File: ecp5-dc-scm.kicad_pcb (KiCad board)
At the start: 6 copper layers, 90 x 120.4 mm, 361 parts, among them IC1 TPS54561, J1 12V_EXT, J10 61301021121, J11 1-2199230-6, J2 S2B-PH-K-S_LF__SN_, J3 2X05, J4 61301021121, J5 61301021121, J6 61301221121, J7 61300611121, J8 SFF-TA-1002-4C+, J9 543630489, Q1 2N7002, Q2 2N7002, Q3 2N7002, Q4 2N7002, Q5 2N7002, Q6 2N7002, Q7 2N7002, U1 ECP5UM5G_85_CABGA756, U10 TPS62823DLCT, U11 W25Q32JVSSIQ_TR, U12 TPS51200DRC, U13 AS4C256M16D3, U14 W25Q32JVSSIQ_TR, U15 W25Q32JVSSIQ_TR, U16 W25Q32JVSSIQ_TR, U2 KSZ9031RNXCA, U3 LM3881MME_NOPB, U4 LM21212-2, U5 TPS71710DCKT, U6 NVT2008DQ,115, U7 TPS62823DLCT, U8 TPS62823DLCT, U9 TPS62823DLCT, Y1 ABM8G-25.000MHZ-18-D2Y-T

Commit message: Add initial component placement
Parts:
- removed the R66 at (353.6, 117.9)
- removed the U16 at (382.4, 132.6)
- removed the U6 at (372.8, 115.2)
- added R53: R_10k_0402, antmicro-footprints:0402-res, F.Cu at (-130.0, 63.7)
- added R75: R_200k_0402, antmicro-footprints:0402-res, F.Cu at (-81.9, 166.2)
- added U11: NVT2008DQ,115, antmicro-footprints:QFN50P250X450X100-21N, F.Cu at (70.0, 159.5)
- added U17: W25Q32JVSSIQ_TR, antmicro-footprints:SOIC-8_W5.6mm, F.Cu at (106.9, 237.0)
- added U5: SN74LVC1G14DBVR, antmicro-footprints:SOT-753, F.Cu at (-133.8, 65.4)
- R74: value R_200k_0402 -> R_357k_0402
- moved C1 497.7 mm to (-84.4, 21.7)
- moved C10 497.7 mm to (-87.3, 15.7)
- moved C11 497.7 mm to (-84.4, 13.7)
- moved C12 497.7 mm to (-93.1, 21.7)
- moved C13 497.7 mm to (-90.2, 19.7)
- moved C14 497.7 mm to (-87.3, 17.7)
- moved C15 497.7 mm to (-84.4, 15.7)
- moved C16 497.7 mm to (-93.1, 23.7)
- moved C17 497.7 mm to (-81.5, 13.7)
- moved C18 497.7 mm to (-81.5, 17.7)
- moved C19 497.7 mm to (-93.1, 15.7)
- moved C2 497.7 mm to (-87.3, 19.7)
- moved C20 497.7 mm to (-84.4, 17.7)
- moved C21 497.7 mm to (-93.1, 25.7)
- moved C22 497.7 mm to (-81.5, 15.7)
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- renumbered R99 to R100, R100 to R101, R101 to R102, R102 to R103, R103 to R104, R104 to R105, R105 to R106, R106 to R107, R53 to R54, R54 to R55, R55 to R56, R56 to R57, R57 to R58, R58 to R59, R59 to R60, R60 to R61, R61 to R62, R62 to R63, R63 to R64, R64 to R65, R65 to R66, R75 to R76, R76 to R77, R77 to R78, R78 to R79, R79 to R80, R80 to R81, R81 to R82, R82 to R83, R83 to R84, R84 to R85, R85 to R86, R86 to R87, R87 to R88, R88 to R89, R89 to R90, R90 to R91, R91 to R92, R92 to R93, R93 to R94, R94 to R95, R95 to R96, R96 to R97, R97 to R98, R98 to R99, U11 to U14, U14 to U15, U15 to U16, U5 to U6
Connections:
- net /Power supply/1V0_EN renamed 1V0_EN
- net Net-(J9-Pad20) renamed ROT_RDY
- C13 pad 1: VCC1V35 -> VCC3V3
- C14 pad 1: VCC1V35 -> VCC3V3
- C15 pad 1: VCC1V35 -> VCC3V3
- C16 pad 1: VCC1V35 -> VCC3V3
- C18 pad 1: VCC1V35 -> VCC3V3
- J6 pad 10: I3C[1]_SCL -> I3C[1]_SCL_1V0
- J6 pad 11: I3C[0]_SDA -> I3C[0]_SDA_1V0
- J6 pad 12: I3C[1]_SDA -> I3C[1]_SDA_1V0
- J6 pad 5: I3C[2]_SCL -> I3C[2]_SCL_1V0
- J6 pad 6: I3C[3]_SCL -> I3C[3]_SCL_1V0
- J6 pad 7: I3C[2]_SDA -> I3C[2]_SDA_1V0
- J6 pad 8: I3C[3]_SDA -> I3C[3]_SDA_1V0
- J6 pad 9: I3C[0]_SCL -> I3C[0]_SCL_1V0
- R67 pad 2: I3C[0]_SCL_3V3 -> I3C[0]_SDA_3V3
- R68 pad 2: I3C[1]_SDA_3V3 -> I3C[0]_SCL_3V3
- R69 pad 2: I3C[1]_SCL_3V3 -> I3C[1]_SDA_3V3
- R70 pad 2: I3C[2]_SDA_3V3 -> I3C[1]_SCL_3V3
- R71 pad 2: I3C[2]_SCL_3V3 -> I3C[2]_SDA_3V3
- R72 pad 2: I3C[3]_SDA_3V3 -> I3C[2]_SCL_3V3
- R73 pad 2: I3C[3]_SCL_3V3 -> I3C[3]_SDA_3V3
- R74 pad 2: /Interfaces/1V0_EN -> I3C[3]_SCL_3V3
- U1 pad A10: Net-(U1-PadA10) -> QSPI1_D3
- U1 pad A14: RGMII_TXD0 -> Net-(U1-PadA14)
- U1 pad A15: RGMII_TX_CLK -> Net-(U1-PadA15)
- U1 pad A16: RGMII_RX_DV -> SGPIO1_DI
- U1 pad A17: RGMII_REF_CLK -> SGPIO0_LD
- U1 pad A19: QSPI1_D3 -> Net-(U1-PadA19)
- U1 pad A20: USB1_DN -> Net-(U1-PadA20)
- U1 pad A22: I3C2_SCL -> I3C[2]_SCL_3V3
- U1 pad A23: I3C0_SDA -> I3C[0]_SDA_3V3
- U1 pad A24: I2C9_SCL -> I2C[9]_SCL
- U1 pad A25: I2C7_SCL -> I2C[7]_SCL
- U1 pad A26: I2C5_SDA -> I2C[5]_SDA
- U1 pad A28: I2C3_SDA -> I2C[3]_SDA
- U1 pad A29: I2C2_SDA -> I2C[2]_SDA
- U1 pad A30: I2C1_SCL -> I2C[1]_SCL
- U1 pad A31: I2C0_SCL -> I2C[0]_SCL
- U1 pad A7: Net-(U1-PadA7) -> USB1_DN
- U1 pad AB1: Net-(U1-PadAB1) -> ETH_MDIO
- U1 pad AB2: Net-(U1-PadAB2) -> RGMII_TXD0
- U1 pad AB3: Net-(U1-PadAB3) -> RGMII_RXD0
- U1 pad AB4: Net-(U1-PadAB4) -> ETH_~RESET
- U1 pad AC1: Net-(U1-PadAC1) -> RGMII_TXD3
- U1 pad AC2: Net-(U1-PadAC2) -> RGMII_TX_DV
- U1 pad AC3: Net-(U1-PadAC3) -> RGMII_TXD2
- U1 pad AC5: Net-(U1-PadAC5) -> RGMII_RXD1
- U1 pad AD1: Net-(U1-PadAD1) -> RGMII_TX_CLK
- U1 pad AD3: Net-(U1-PadAD3) -> RGMII_TX_CLK
- U1 pad AD4: Net-(U1-PadAD4) -> ETH_INT_N
- U1 pad AD6: Net-(U1-PadAD6) -> ETH_MDC
- U1 pad AE1: Net-(U1-PadAE1) -> RGMII_RXD2
- U1 pad AE2: Net-(U1-PadAE2) -> RGMII_TXD1
- U1 pad AE3: Net-(U1-PadAE3) -> RGMII_RXD3
- U1 pad AE4: Net-(U1-PadAE4) -> RGMII_RX_DV
- U1 pad AE5: Net-(U1-PadAE5) -> RGMII_RX_CLK
- U1 pad AE6: Net-(U1-PadAE6) -> RGMII_REF_CLK
- U1 pad AG5: (no net) -> JTAG_TDO
- U1 pad AJ5: (no net) -> JTAG_TDI
- U1 pad AK10: (no net) -> Net-(U1-PadAK10)
- U1 pad AK12: (no net) -> Net-(U1-PadAK12)
- U1 pad AK13: (no net) -> Net-(U1-PadAK13)
- U1 pad AK18: (no net) -> Net-(U1-PadAK18)
- U1 pad AK19: (no net) -> Net-(U1-PadAK19)
- U1 pad AK21: (no net) -> Net-(U1-PadAK21)
- U1 pad AK22: (no net) -> Net-(U1-PadAK22)
- U1 pad AK5: (no net) -> JTAG_TCK
- U1 pad AK9: (no net) -> Net-(U1-PadAK9)
- U1 pad AM11: (no net) -> Net-(U1-PadAM11)
- U1 pad AM12: (no net) -> Net-(U1-PadAM12)
- U1 pad AM14: (no net) -> Net-(U1-PadAM14)
- U1 pad AM15: (no net) -> Net-(U1-PadAM15)
- U1 pad AM17: (no net) -> Net-(U1-PadAM17)
- U1 pad AM18: (no net) -> Net-(U1-PadAM18)
- U1 pad AM20: (no net) -> Net-(U1-PadAM20)
- U1 pad AM21: (no net) -> Net-(U1-PadAM21)
- U1 pad AM23: (no net) -> Net-(U1-PadAM23)
- U1 pad AM24: (no net) -> Net-(U1-PadAM24)
- U1 pad AM5: (no net) -> JTAG_TMS
- U1 pad AM8: (no net) -> Net-(U1-PadAM8)
- U1 pad AM9: (no net) -> Net-(U1-PadAM9)
- U1 pad B11: Net-(U1-PadB11) -> QSPI1_D2
- U1 pad B14: ETH_MDIO -> Net-(U1-PadB14)
- U1 pad B16: RGMII_RXD1 -> SGPIO1_LD
- U1 pad B17: ETH_MDC -> SGPIO0_DI
- U1 pad B19: QSPI1_D0 -> Net-(U1-PadB19)
- U1 pad B22: I3C1_SCL -> I3C[1]_SCL_3V3
- U1 pad B23: I2C12_SDA -> I2C[12]_SDA
- U1 pad B25: I2C6_SCL -> I2C[6]_SCL
- U1 pad B26: I2C4_SDA -> I2C[4]_SDA
- U1 pad B29: I2C1_SDA -> I2C[1]_SDA
- U1 pad B30: I2C0_SDA -> I2C[0]_SDA
- U1 pad B32: Net-(U1-PadB32) -> ESPI_CLK
- U1 pad B7: Net-(U1-PadB7) -> USB2_DN
- U1 pad C11: Net-(U1-PadC11) -> QSPI1_CS_N
- U1 pad C14: RGMII_TXD3 -> Net-(U1-PadC14)
- U1 pad C15: RGMII_TXD2 -> Net-(U1-PadC15)
- U1 pad C16: RGMII_RXD0 -> SGPIO1_DO
- U1 pad C17: RGMII_RX_CLK -> SGPIO0_DO
- U1 pad C19: QSPI1_D2 -> Net-(U1-PadC19)
- U1 pad C20: I3C3_SCL -> I3C[3]_SCL_3V3
- U1 pad C22: I3C2_SDA -> I3C[2]_SDA_3V3
- U1 pad C23: I2C11_SCL -> I2C[11]_SCL
- U1 pad C24: I2C8_SCL -> I2C[8]_SCL
- U1 pad C25: I2C7_SDA -> I2C[7]_SDA
- U1 pad C26: I2C3_SCL -> I2C[3]_SCL
- U1 pad C28: Net-(U1-PadC28) -> ESPI_RESET_N
- U1 pad C29: Net-(U1-PadC29) -> ESPI_IO3
- U1 pad C30: Net-(U1-PadC30) -> ESPI_IO2
- U1 pad D11: Net-(U1-PadD11) -> QSPI1_D0
- U1 pad D14: RGMII_RXD2 -> Net-(U1-PadD14)
- U1 pad D15: RGMII_TX_DV -> Net-(U1-PadD15)
- U1 pad D16: ETH_~RESET -> SGPIO_RESET_N
- U1 pad D17: Net-(U1-PadD17) -> SGPIO_CLK
- U1 pad D18: QSPI1_D1 -> Net-(U1-PadD18)
- U1 pad D19: USB2_DN -> Net-(U1-PadD19)
- U1 pad D20: USB1_DP -> Net-(U1-PadD20)
- U1 pad D22: I3C1_SDA -> I3C[1]_SDA_3V3
- U1 pad D23: I2C10_SCL -> I2C[10]_SCL
- U1 pad D24: I2C9_SDA -> I2C[9]_SDA
- U1 pad D25: I2C6_SDA -> I2C[6]_SDA
- U1 pad D26: I2C2_SCL -> I2C[2]_SCL
- U1 pad D28: Net-(U1-PadD28) -> ESPI_ALERT_N
- U1 pad D29: Net-(U1-PadD29) -> ESPI_IO1
- U1 pad E11: Net-(U1-PadE11) -> QSPI1_CLK
- U1 pad E14: RGMII_TX_CLK -> Net-(U1-PadE14)
- U1 pad E16: ETH_INT_N -> SGPIO_INTR_N
- U1 pad E19: QSPI1_CS_N -> Net-(U1-PadE19)
- U1 pad E22: I3C0_SCL -> I3C[0]_SCL_3V3
- U1 pad E23: I2C11_SDA -> I2C[11]_SDA
- U1 pad E25: I2C5_SCL -> I2C[5]_SCL
- U1 pad E29: Net-(U1-PadE29) -> ESPI_CS1_N
- U1 pad E8: Net-(U1-PadE8) -> USB1_DP
- U1 pad F11: Net-(U1-PadF11) -> QSPI1_D1
- U1 pad F15: RGMII_TXD1 -> Net-(U1-PadF15)
- U1 pad F16: RGMII_RXD3 -> Net-(U1-PadF16)
- U1 pad F18: QSPI1_CLK -> Net-(U1-PadF18)
- U1 pad F19: USB2_DP -> Net-(U1-PadF19)
- U1 pad F20: I3C3_SDA -> I3C[3]_SDA_3V3
- U1 pad F22: I2C12_SCL -> I2C[12]_SCL
- U1 pad F23: I2C10_SDA -> I2C[10]_SDA
- U1 pad F24: I2C8_SDA -> I2C[8]_SDA
- U1 pad F25: I2C4_SCL -> I2C[4]_SCL
- U1 pad F28: Net-(U1-PadF28) -> ESPI_CS0_N
- U1 pad F29: Net-(U1-PadF29) -> ESPI_IO0
- U1 pad F8: Net-(U1-PadF8) -> USB2_DP
- U1 pad H27: ESPI_IO3 -> Net-(U1-PadH27)
- U1 pad H28: ESPI_IO1 -> Net-(U1-PadH28)
- U1 pad H30: JTAG_TCK -> Net-(U1-PadH30)
- U1 pad H31: JTAG_TDI -> Net-(U1-PadH31)
- U1 pad H32: JTAG_TDO -> Net-(U1-PadH32)
- U1 pad J26: ESPI_IO2 -> Net-(U1-PadJ26)
- U1 pad J27: ESPI_IO0 -> Net-(U1-PadJ27)
- U1 pad J30: JTAG_TMS -> Net-(U1-PadJ30)
- U1 pad K26: ESPI_CLK -> Net-(U1-PadK26)
- U1 pad K27: ESPI_CS1_N -> Net-(U1-PadK27)
- U1 pad K28: ESPI_CS0_N -> Net-(U1-PadK28)
- U1 pad K29: ESPI_ALERT_N -> Net-(U1-PadK29)
- U1 pad L26: SGPIO1_LD -> Net-(U1-PadL26)
- U1 pad L27: SGPIO1_DI -> Net-(U1-PadL27)
- U1 pad L29: SGPIO_INTR_N -> Net-(U1-PadL29)
- U1 pad L30: ESPI_RESET_N -> Net-(U1-PadL30)
- U1 pad M23: VCC1V35 -> VCC3V3
- U1 pad N26: SGPIO0_DI -> Net-(U1-PadN26)
- U1 pad N27: SGPIO0_LD -> Net-(U1-PadN27)
- U1 pad N29: SGPIO1_DO -> Net-(U1-PadN29)
- U1 pad N30: SGPIO_RESET_N -> Net-(U1-PadN30)
- U1 pad P23: VCC1V35 -> VCC3V3
- U1 pad P26: SGPIO_CLK -> Net-(U1-PadP26)
- U1 pad P27: SGPIO0_DO -> Net-(U1-PadP27)
- U1 pad R23: VCC1V35 -> VCC3V3
- U1 pad T23: VCC1V35 -> VCC3V3
- U3 pad 4: GND -> Net-(C124-Pad1)
- U3 pad 5: Net-(C124-Pad1) -> GND
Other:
- board text added: "DDR3"
- board text added: "Ethernet"
- board text added: "I2C"
- board text added: "I3C"
- board text added: "JTAG"
- board text added: "M.2 SSD"
- board text added: "Power supply"
- board text added: "ROT module"
- board text added: "TPM"

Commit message: Update PCB layout
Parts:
- removed the C122 at (-96.7, 80.0)
- removed the C123 at (-89.4, 68.8)
- removed the C125 at (-86.5, 64.8)
- removed C131: C_1n8_0402, antmicro-footprints:0402-cap
- removed the C133 at (-96.4, 82.0)
- removed the C134 at (-106.1, 87.8)
- removed the C135 at (-93.0, 63.6)
- removed the C137 at (-109.9, 90.1)
- removed the C142 at (-95.3, 76.0)
- removed the C150 at (-102.2, 82.0)
- removed the C154 at (-99.3, 84.0)
- removed the C157 at (-104.1, 89.9)
- removed the J1 at (72.4, 73.0)
- removed L6: 470n/IHLP1212, Inductor_SMD:L_Vishay_IHLP-1212
- removed the R17 at (-103.8, 72.3)
- removed the R18 at (-89.0, 74.8)
- removed the R19 at (-94.8, 71.8)
- removed the R22 at (-101.1, 76.0)
- removed the R23 at (-92.3, 67.8)
- removed the R24 at (-86.6, 62.8)
- removed the R25 at (-108.0, 83.8)
- removed the R31 at (-97.7, 74.0)
- removed the R45 at (-107.0, 90.1)
- removed the R46 at (-104.0, 76.5)
- removed the R47 at (-95.2, 67.8)
- removed the R49 at (-89.5, 60.9)
- removed the R53 at (-130.0, 63.7)
- removed the R58 at (-97.7, 72.0)
- removed the R59 at (-105.5, 79.9)
- removed TP2: TP_SMD1MM, antmicro-footprints:Testpoint_smd_1mm
- removed the U4 at (85.9, 83.0)
- removed the U5 at (-133.8, 65.4)
- added C144: C_10u_0402, antmicro-footprints:0402-cap, F.Cu at (37.2, 67.8)
- added C145: C_120p_0402, antmicro-footprints:0402-res, F.Cu at (47.7, 57.4)
- added C147: C_10u_0402, antmicro-footprints:0402-cap, F.Cu at (34.3, 67.6)
- added J2: DC_SOCKET, antmicro-footprints:DC_SOCKET, F.Cu at (71.1, 59.0)
- added Q10: IRLML6402TRPBF, antmicro-footprints:SOT-23-3, F.Cu at (30.3, 64.5)
- added Q11: IRLML6402TRPBF, antmicro-footprints:SOT-23-3, F.Cu at (35.0, 64.2)
- added Q13: IRLML6402TRPBF, antmicro-footprints:SOT-23-3, F.Cu at (39.7, 58.9)
- added Q5: IRLML6402TRPBF, antmicro-footprints:SOT-23-3, F.Cu at (39.7, 53.9)
- added Q7: IRLML6402TRPBF, antmicro-footprints:SOT-23-3, F.Cu at (35.0, 59.2)
- added Q8: IRLML6402TRPBF, antmicro-footprints:SOT-23-3, F.Cu at (44.4, 53.9)
- added R37: R_124k_0402, antmicro-footprints:0402-res, F.Cu at (40.1, 67.8)
- added R42: R_124k_0402, antmicro-footprints:0402-res, F.Cu at (47.7, 59.4)
- added R43: R_100k_0402, antmicro-footprints:0402-res, F.Cu at (46.6, 62.0)
- added U11: TPS62823DLCT, antmicro-footprints:QFN-8_2x1mm, F.Cu at (99.5, 96.8)
- added U7: SN74LVC1G08DCKR, antmicro-footprints:SC-70-5, F.Cu at (44.1, 58.7)
- added U9: SN74LVC1G04DBVR, antmicro-footprints:SOT-753, F.Cu at (30.3, 54.1)
- C146: value C_120p_0402 -> C_10u_0402; footprint antmicro-footprints:0402-res -> antmicro-footprints:0402-cap
- L1: value XAL5030-801 -> IHLP1212AEERR47M11; footprint antmicro-footprints:Coilcraft-XAL5030 -> antmicro-footprints:IHLP-1212AE
- L3, L4, L5: value 470n/IHLP1212 -> IHLP1212AEERR47M11; footprint Inductor_SMD:L_Vishay_IHLP-1212 -> antmicro-footprints:IHLP-1212AE
- R32: value R_470k_0402 -> R_200k_0402
- U13: footprint Package_BGA:BGA-96_9.0x13.0mm_Layout2x3x16_P0.8mm -> antmicro-footprints:BGA-96_9.0x13.0mm_Layout2x3x16_P0.8mm
- U6: value TPS71710DCKT -> SN74LVC1G04DBVR; footprint antmicro-footprints:SOT65P210X110-5N -> antmicro-footprints:SOT-753
- U8: value TPS62823DLCT -> SN74LVC1G04DBVR; footprint antmicro-footprints:QFN-8_2x1mm -> antmicro-footprints:SOT-753
- moved U6 166.7 mm to (35.0, 54.1)
- moved L5 156.0 mm to (22.9, 69.1)
- moved C146 154.6 mm to (43.7, 62.0)
- moved L4 152.1 mm to (30.4, 67.9)
- moved R32 143.5 mm to (43.1, 64.0)
- moved L3 124.9 mm to (18.0, 69.1)
- moved U8 72.0 mm to (30.3, 59.4), turned to 0 degrees
- moved L1 46.9 mm to (39.8, 62.2), turned to 0 degrees
- moved U13 1.04 mm to (81.8, 115.8)
- renumbered C30 to C1, C29 to C10, C102 to C101, C104 to C102, C107 to C103, C110 to C104, C113 to C105, C114 to C106, C116 to C107, C118 to C108, C105 to C109, C1 to C11, C108 to C110, C117 to C112, C119 to C113, C120 to C114, C101 to C115, C103 to C116, C106 to C117, C109 to C118, C112 to C119, C2 to C12, C115 to C120, C141 to C122, C145 to C123, C149 to C124, C153 to C125, C136 to C126, C138 to C127, C139 to C128, C140 to C129, C3 to C13, C129 to C133, C128 to C134, C130 to C135, C143 to C136, C147 to C137, C151 to C138, C155 to C139, C4 to C14, C144 to C140, C148 to C141, C152 to C142, C156 to C143, C124 to C148, C166 to C149, C5 to C15, C167 to C150, C169 to C151, C171 to C152, C173 to C153, C176 to C154, C178 to C155, C168 to C156, C170 to C157, C172 to C158, C174 to C159, C6 to C16, C177 to C160, C179 to C161, C175 to C162, C180 to C163, C158 to C164, C159 to C165, C161 to C166, C163 to C167, C164 to C168, C181 to C169, C7 to C17, C165 to C170, C160 to C171, C162 to C172, C182 to C173, C186 to C174, C185 to C175, C184 to C176, C183 to C177, C187 to C178, C189 to C179, C8 to C18, C188 to C180, C190 to C181, C191 to C182, C192 to C183, C193 to C184, C194 to C185, C9 to C19, C31 to C2, C11 to C20, C13 to C21, C14 to C22, C15 to C23, C16 to C24, C18 to C25, C20 to C26, C21 to C27, C22 to C28, C23 to C29, C32 to C3, C24 to C30, C10 to C31, C12 to C32, C17 to C33, C19 to C34, C56 to C35, C59 to C36, C62 to C37, C65 to C38, C68 to C39, C33 to C4, C71 to C40, C74 to C41, C77 to C42, C80 to C43, C83 to C44, C85 to C45, C87 to C46, C89 to C47, C90 to C48, C91 to C49, C34 to C5, C92 to C50, C93 to C51, C94 to C52, C95 to C53, C35 to C54, C36 to C55, C37 to C56, C38 to C57, C39 to C58, C40 to C59, C25 to C6, C43 to C60, C46 to C61, C51 to C62, C57 to C63, C60 to C64, C63 to C65, C69 to C67, C72 to C68, C75 to C69, C26 to C7, C78 to C70, C81 to C71, C41 to C72, C44 to C73, C47 to C74, C52 to C75, C48 to C76, C53 to C77, C58 to C78, C61 to C79, C27 to C8, C64 to C80, C67 to C81, C70 to C82, C73 to C83, C76 to C84, C79 to C85, C82 to C86, C84 to C87, C86 to C88, C88 to C89, C28 to C9, C42 to C90, C45 to C91, C49 to C92, C54 to C93, C50 to C94, C55 to C95, D8 to D1, D6 to D2, D2 to D3, D5 to D4, D7 to D5, D4 to D6, D1 to D7, D3 to D8, F2 to F1, F1 to F2, FB4 to FB2, FB2 to FB3, FB5 to FB4, FB3 to FB5, FB7 to FB6, FB6 to FB7, J?1 to J1, J9 to J11, J11 to J12, J2 to J3, J7 to J6, J3 to J7, J6 to J8, J8 to J9, Q7 to Q1, Q2 to Q12, Q5 to Q2, Q4 to Q3, Q6 to Q4, Q3 to Q6, Q1 to Q9, R15 to R1, R6 to R10, R7 to R11, R8 to R12, R9 to R13, R10 to R14, R11 to R15, R12 to R16, R42 to R17, R37 to R18, R40 to R19, R16 to R2, R35 to R20, R43 to R21, R26 to R22, R27 to R23, R44 to R24, R21 to R25, R28 to R26, R39 to R27, R29 to R28, R20 to R29, R14 to R3, R34 to R30, R30 to R31, R41 to R33, R48 to R34, R36 to R35, R38 to R36, R33 to R38, R50 to R39, R13 to R4, R56 to R40, R54 to R41, R57 to R44, R55 to R45, R66 to R46, R60 to R47, R51 to R48, R52 to R49, R1 to R5, R61 to R50, R65 to R51, R64 to R52, R63 to R53, R62 to R54, R75 to R55, R67 to R56, R69 to R57, R71 to R58, R73 to R59, R2 to R6, R68 to R60, R70 to R61, R72 to R62, R74 to R63, R79 to R64, R83 to R65, R87 to R66, R91 to R67, R95 to R68, R99 to R69, R3 to R7, R101 to R70, R102 to R71, R100 to R72, R103 to R73, R78 to R74, R82 to R75, R86 to R76, R90 to R77, R94 to R78, R98 to R79, R4 to R8, R77 to R80, R85 to R82, R89 to R83, R93 to R84, R97 to R85, R76 to R86, R80 to R87, R84 to R88, R88 to R89, R5 to R9, R92 to R90, R96 to R91, R104 to R92, R106 to R93, R107 to R94, R105 to R95, U3 to U12, U12 to U14, U11 to U15, U17 to U16, U16 to U17, U15 to U18, U14 to U19, U7 to U3, U9 to U4, U10 to U5
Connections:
- C137 pad 2: Net-(C147-Pad2) -> Net-(C137-Pad2)
- C146 pad 1: VCC2V5 -> VCC1V0
- C146 pad 2: Net-(C146-Pad2) -> GND
- L1 pad 2: +1V2 -> VCC3V3
- L3 pad 2: VCC3V3 -> VCC1V8
- L4 pad 2: VCC2V5 -> VCC1V35
- L5 pad 2: VCC1V8 -> VCC1V0
- Q9 pad 1: GND -> /Power supply/1V0_PG
- R32 pad 1: Net-(C134-Pad2) -> VCC1V8
- R32 pad 2: Net-(C133-Pad1) (its old number) -> Net-(C137-Pad2)
- R34 pad 1: Net-(C147-Pad2) -> Net-(C137-Pad2)
- R41 pad 2: GND -> /Power supply/1V0_PG
- U12 pad 6: 1V0_EN -> /Power supply/VCCIO_EN
- U12 pad 7: /Power supply/1V2_EN -> /Power supply/VCCAUX_EN
- U12 pad 8: /Power supply/3V3_EN -> /Power supply/VCCINT_EN
- U3 pad 6: Net-(L3-Pad1) -> Net-(L1-Pad1)
- U4 pad 1: /Power supply/1V2_EN -> /Power supply/1V8_EN
- U4 pad 2: Net-(C147-Pad2) -> Net-(C137-Pad2)
- U4 pad 6: Net-(L5-Pad1) -> Net-(L3-Pad1)
- U5 pad 1: /Power supply/1V2_EN -> /Power supply/1V35_EN
- U5 pad 6: Net-(L6-Pad1) -> Net-(L4-Pad1)
- U6 pad 1: VCC3V3 -> Net-(U6-Pad1)
- U6 pad 2: GND -> /Power supply/VCCINT_EN
- U6 pad 3: 1V0_EN -> GND
- U6 pad 4: Net-(R58-Pad2) -> /Power supply/VCCINT_EN_N
- U6 pad 5: VCC1V0 -> VCC3V3
- U8 pad 1: /Power supply/1V2_EN -> Net-(U8-Pad1)
- U8 pad 2: Net-(C146-Pad2) -> /Power supply/VCCAUX_EN
- U8 pad 4: (no net) -> /Power supply/VCCAUX_EN_N
- U8 pad 5: GND -> VCC3V3

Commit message: Clean up main sch file
Separate power supply schematic
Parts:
- removed the C1 at (-78.6, 15.7)
- removed the C10 at (-90.2, 25.7)
- removed the C11 at (-84.4, 21.7)
- removed the C12 at (-87.3, 19.7)
- removed the C13 at (-90.2, 13.7)
- removed the C14 at (-93.1, 17.7)
- removed the C15 at (-90.2, 15.7)
- removed the C16 at (-87.3, 13.7)
- removed the C17 at (-93.1, 19.7)
- removed the C18 at (-90.2, 17.7)
- removed the C19 at (-93.1, 13.7)
- removed the C2 at (-87.3, 23.7)
- removed the C20 at (-84.4, 13.7)
- removed the C21 at (-90.2, 19.7)
- removed the C22 at (-87.3, 17.7)
- removed the C23 at (-84.4, 15.7)
- removed the C24 at (-93.1, 23.7)
- removed the C25 at (-81.5, 17.7)
- removed the C26 at (-84.4, 17.7)
- removed the C27 at (-93.1, 25.7)
- removed the C28 at (-81.5, 15.7)
- removed the C29 at (-90.2, 23.7)
- removed the C3 at (-93.1, 29.7)
- removed the C30 at (-78.6, 13.7)
- removed the C31 at (-87.3, 15.7)
- removed the C32 at (-93.1, 21.7)
- removed the C33 at (-81.5, 13.7)
- removed the C34 at (-93.1, 15.7)
- removed the C35 at (68.7, -24.3)
- removed the C36 at (79.0, -31.9)
- removed the C37 at (75.5, -29.4)
- removed the C38 at (82.6, -34.4)
- removed the C39 at (81.3, -29.9)
- removed the C4 at (-75.7, 13.7)
- removed the C40 at (77.7, -25.5)
- removed the C41 at (81.3, -27.9)
- removed the C42 at (89.4, -22.4)
- removed the C43 at (87.1, -24.4)
- removed the C44 at (83.5, -20.0)
- removed the C45 at (92.9, -28.4)
- removed the C46 at (92.9, -26.4)
- removed the C47 at (87.7, -32.4)
- removed the C48 at (92.9, -24.4)
- removed the C49 at (89.4, -20.5)
- removed the C5 at (-90.2, 27.7)
- removed the C50 at (71.9, -23.0)
- removed the C51 at (80.6, -20.0)
- removed the C52 at (78.4, -29.4)
- removed the C53 at (75.5, -27.5)
- removed the C54 at (68.7, -34.1)
- removed the C55 at (81.3, -25.9)
- removed the C56 at (91.3, -34.4)
- removed the C57 at (77.7, -21.5)
- removed the C58 at (84.2, -27.9)
- removed the C59 at (87.1, -30.4)
- removed the C6 at (-93.1, 27.7)
- removed the C60 at (80.6, -24.0)
- removed the C61 at (80.6, -22.0)
- removed the C62 at (93.6, -32.4)
- removed the C63 at (79.3, -34.1)
- removed C65, C66, C67: C_470n_0402, antmicro-footprints:0402-cap
- removed the C7 at (-87.3, 21.7)
- removed the C8 at (-84.4, 19.7)
- removed the C9 at (-90.2, 21.7)
- removed the D1 at (-107.4, 75.6)
- removed the FB1 at (68.7, -31.7)
- removed the FB2 at (68.7, -26.7)
- removed the FB3 at (72.2, -34.1)
- removed the J2 at (71.1, 59.0)
- removed the J3 at (-121.0, 62.0)
- removed Q13: IRLML6402TRPBF, antmicro-footprints:SOT-23-3
- removed the R17 at (-108.7, 81.8)
- removed the R18 at (-89.4, 66.8)
- removed the R19 at (-92.3, 65.8)
- removed the R20 at (-95.3, 78.0)
- removed the R21 at (-100.6, 74.0)
- removed the R22 at (-105.8, 81.8)
- removed the R23 at (-89.4, 64.8)
- removed the R24 at (-100.6, 72.0)
- removed the R25 at (-108.4, 79.9)
- removed the R26 at (-112.8, 89.0)
- removed the R27 at (-110.9, 84.1)
- removed the R28 at (-101.1, 78.0)
- removed the R29 at (-96.0, 69.8)
- removed the R30 at (-86.5, 68.8)
- removed the R31 at (-93.1, 69.8)
- removed the R32 at (43.1, 64.0)
- removed the R33 at (-89.5, 62.8)
- removed the R34 at (-114.8, 87.0)
- removed the R35 at (-102.2, 84.0)
- removed the R36 at (-118.7, 89.9)
- removed the R37 at (40.1, 67.8)
- removed the R38 at (-89.0, 70.8)
- removed the R39 at (-95.2, 65.8)
- removed the R40 at (-86.6, 60.9)
- removed the R41 at (-104.0, 74.5)
- removed the R42 at (47.7, 59.4)
- removed the R43 at (46.6, 62.0)
- removed the R44 at (-111.9, 87.0)
- removed the R45 at (-107.9, 77.9)
- removed the U1 at (105.5, 119.5)
- removed the U3 at (99.5, 83.7)
- removed the U4 at (99.5, 92.3)
- removed the U5 at (99.5, 88.0)
- removed the U6 at (35.0, 54.1)
- removed the U7 at (44.1, 58.7)
- removed the U8 at (30.3, 59.4)
- added C100: C_4u7_0402, antmicro-footprints:0402-cap, F.Cu at (-3.94, 60.5)
- added C101: C_4u7_0402, antmicro-footprints:0402-cap, F.Cu at (-10.4, 67.0)
- added C102: C_10n_0402, antmicro-footprints:0402-cap, F.Cu at (2.52, 54.1)
- added C103: C_470n_0402, antmicro-footprints:0402-cap, F.Cu at (5.43, 51.6)
- added C104: C_10n_0402, antmicro-footprints:0402-cap, F.Cu at (-3.30, 52.6)
- added C105: C_470n_0402, antmicro-footprints:0402-cap, F.Cu at (6.07, 49.6)
- added C106: C_10n_0402, antmicro-footprints:0402-cap, F.Cu at (-13.3, 62.0)
- added C107: C_1n_0402, antmicro-footprints:0402-res, F.Cu at (-9.76, 59.0)
- added C108: C_10n_0402, antmicro-footprints:0402-cap, F.Cu at (0.25, 50.1)
- added C109: C_1n_0402, antmicro-footprints:0402-res, F.Cu at (-6.21, 54.6)
- added C110: C_10n_0402, antmicro-footprints:0402-cap, F.Cu at (-13.3, 71.9)
- added C111: C_1n_0402, antmicro-footprints:0402-res, F.Cu at (-1.67, 64.0)
- added C112: C_47u_0603, antmicro-footprints:0603-cap, F.Cu at (-9.44, 47.9)
- added C113: C_47u_0603, antmicro-footprints:0603-cap, F.Cu at (-13.0, 52.8)
- added C114: C_47u_0603, antmicro-footprints:0603-cap, F.Cu at (-9.44, 50.3)
- added C115: C_4u7_0402, antmicro-footprints:0402-cap, F.Cu at (-7.49, 66.5)
- added C116: C_4u7_0402, antmicro-footprints:0402-cap, F.Cu at (-6.85, 56.5)
- added C117: C_4u7_0402, antmicro-footprints:0402-cap, F.Cu at (1.88, 60.0)
- added C118: C_4u7_0402, antmicro-footprints:0402-cap, F.Cu at (-1.03, 62.0)
- added C119: C_470n_0402, antmicro-footprints:0402-cap, F.Cu at (-13.3, 73.9)
- added C120: C_470n_0402, antmicro-footprints:0402-cap, F.Cu at (-7.49, 68.5)
- added C121: C_470n_0402, antmicro-footprints:0402-cap, F.Cu at (5.43, 55.6)
- added C130: C_470n_0402, antmicro-footprints:0402-cap, F.Cu at (2.52, 52.1)
- added C131: C_10n_0402, antmicro-footprints:0402-cap, F.Cu at (-0.39, 54.1)
- added C132: C_470n_0402, antmicro-footprints:0402-cap, F.Cu at (-6.85, 60.5)
- added C149: C_470n_0402, antmicro-footprints:0402-cap, F.Cu at (-0.39, 56.1)
- added C150: C_470n_0402, antmicro-footprints:0402-cap, F.Cu at (-13.3, 69.9)
- added C151: C_470n_0402, antmicro-footprints:0402-cap, F.Cu at (-7.49, 64.5)
- added C152: C_4u7_0402, antmicro-footprints:0402-cap, F.Cu at (8.75, 79.6)
- added C153: C_470n_0402, antmicro-footprints:0402-cap, F.Cu at (2.93, 85.5)
- added C154: C_470n_0402, antmicro-footprints:0402-cap, F.Cu at (5.84, 83.5)
- added C155: C_470n_0402, antmicro-footprints:0402-cap, F.Cu at (8.75, 81.6)
- added C156: C_470n_0402, antmicro-footprints:0402-cap, F.Cu at (2.93, 79.6)
- added C157: C_4u7_0402, antmicro-footprints:0402-cap, F.Cu at (2.93, 87.5)
- added C158: C_470n_0402, antmicro-footprints:0402-cap, F.Cu at (8.75, 83.5)
- added C159: C_470n_0402, antmicro-footprints:0402-cap, F.Cu at (2.93, 83.5)
- added C160: C_470n_0402, antmicro-footprints:0402-cap, F.Cu at (5.84, 81.6)
- added C161: C_470n_0402, antmicro-footprints:0402-cap, F.Cu at (5.84, 85.5)
- added C162: C_470n_0402, antmicro-footprints:0402-cap, F.Cu at (11.7, 81.6)
- added C163: C_470n_0402, antmicro-footprints:0402-cap, F.Cu at (14.6, 79.6)
- added C164: C_470n_0402, antmicro-footprints:0402-cap, F.Cu at (5.84, 87.5)
- added C165: C_4u7_0402, antmicro-footprints:0402-cap, F.Cu at (8.75, 85.5)
- added C166: C_470n_0402, antmicro-footprints:0402-cap, F.Cu at (5.84, 79.6)
- added C167: C_470n_0402, antmicro-footprints:0402-cap, F.Cu at (17.5, 83.5)
- added C168: C_470n_0402, antmicro-footprints:0402-cap, F.Cu at (14.6, 81.6)
- added C169: C_470n_0402, antmicro-footprints:0402-cap, F.Cu at (20.4, 81.6)
- added C170: C_470n_0402, antmicro-footprints:0402-cap, F.Cu at (14.6, 87.5)
- added C171: C_4u7_0402, antmicro-footprints:0402-cap, F.Cu at (17.5, 85.5)
- added C172: C_470n_0402, antmicro-footprints:0402-cap, F.Cu at (20.4, 83.5)
- added C173: C_470n_0402, antmicro-footprints:0402-cap, F.Cu at (17.5, 87.5)
- added C174: C_470n_0402, antmicro-footprints:0402-cap, F.Cu at (20.4, 85.5)
- added C175: C_470n_0402, antmicro-footprints:0402-cap, F.Cu at (11.7, 79.6)
- added C176: C_4u7_0402, antmicro-footprints:0402-cap, F.Cu at (14.6, 85.5)
- added C177: C_470n_0402, antmicro-footprints:0402-cap, F.Cu at (2.93, 81.6)
- added C178: C_470n_0402, antmicro-footprints:0402-cap, F.Cu at (11.7, 83.5)
- added C179: C_470n_0402, antmicro-footprints:0402-cap, F.Cu at (11.7, 87.5)
- added C180: C_470n_0402, antmicro-footprints:0402-cap, F.Cu at (20.4, 79.6)
- added C181: C_4u7_0402, antmicro-footprints:0402-cap, F.Cu at (17.5, 81.6)
- added C182: C_470n_0402, antmicro-footprints:0402-cap, F.Cu at (14.6, 83.5)
- added C183: C_470n_0402, antmicro-footprints:0402-cap, F.Cu at (11.7, 85.5)
- added C184: C_470n_0402, antmicro-footprints:0402-cap, F.Cu at (8.75, 87.5)
- added C185: C_470n_0402, antmicro-footprints:0402-cap, F.Cu at (17.5, 79.6)
- added C186: C_10u_0402, antmicro-footprints:0402-cap, F.Cu at (49.4, 47.6)
- added C187: C_10u_0402, antmicro-footprints:0402-cap, F.Cu at (45.9, 59.3)
- added C188: C_100n_0402, antmicro-footprints:0402-cap, F.Cu at (45.1, 51.4)
- added C189: C_10u_0402, antmicro-footprints:0402-cap, F.Cu at (40.2, 53.9)
- added C190: C_120p_0402, antmicro-footprints:0402-res, F.Cu at (30.5, 65.0)
- added C191: C_1n8_0402, antmicro-footprints:0402-cap, F.Cu at (37.2, 57.5)
- added C192: C_10u_0402, antmicro-footprints:0402-cap, F.Cu at (17.3, 68.0)
- added C193: C_180p_0402, antmicro-footprints:0402-cap, F.Cu at (40.2, 55.8)
- added C194: C_10u_0402, antmicro-footprints:0402-cap, F.Cu at (40.1, 57.8)
- added C195: C_750p_0402, antmicro-footprints:0402-res, F.Cu at (48.9, 56.1)
- added C196: C_47u_0603, antmicro-footprints:0603-cap, F.Cu at (26.1, 67.7)
- added C96: C_100n_0402, antmicro-footprints:0402-cap, F.Cu at (-1.03, 58.1)
- added C97: C_47u_0603, antmicro-footprints:0603-cap, F.Cu at (-13.0, 55.3)
- added C98: C_47u_0603, antmicro-footprints:0603-cap, F.Cu at (-13.0, 47.9)
- added C99: C_10n_0402, antmicro-footprints:0402-cap, F.Cu at (-7.49, 62.5)
- added D9: LG_L29K-G2J1-24-Z, antmicro-footprints:LED_0603, F.Cu at (31.0, 62.7)
- added FB6: BLM18PG121SN1D, antmicro-footprints:0603-res, F.Cu at (-9.44, 52.8)
- added FB7: BLM18PG121SN1D, antmicro-footprints:0603-res, F.Cu at (-5.89, 47.9)
- added FB8: BLM18PG121SN1D, antmicro-footprints:0603-res, F.Cu at (-13.0, 50.3)
- added J11: S2B-PH-K-S_LF__SN_, antmicro-footprints:PinHeader_1x2_P2mm_Drill1mm_RA, F.Cu at (72.3, 22.3)
- added L6: 470n/IHLP1212, Inductor_SMD:L_Vishay_IHLP-1212, F.Cu at (22.8, 49.0)
- added L7: XAL5030-801, antmicro-footprints:Coilcraft-XAL5030, F.Cu at (85.9, 66.9)
- added R100: R_1k_0402, antmicro-footprints:0402-res, F.Cu at (40.1, 59.8)
- added R101: R_1k_0402, antmicro-footprints:0402-res, F.Cu at (43.1, 55.8)
- added R102: R_1k_0402, antmicro-footprints:0402-res, F.Cu at (48.0, 50.1)
- added R63: R_1k_0402, antmicro-footprints:0402-res, F.Cu at (86.8, 37.9)
- added R64: R_1k_0402, antmicro-footprints:0402-res, F.Cu at (91.2, 35.7)
- added R65: R_1k_0402, antmicro-footprints:0402-res, F.Cu at (95.6, 31.1)
- added R66: R_16k9_0402, antmicro-footprints:0402-res, F.Cu at (94.1, 33.7)
- added R67: R_243k_0402, antmicro-footprints:0402-res, F.Cu at (89.7, 37.9)
- added R68: R_100k_0402, antmicro-footprints:0402-res, F.Cu at (83.9, 39.7)
- added R69: R_0R_0402, antmicro-footprints:0402-res, F.Cu at (91.8, 29.7)
- added R74: R_100k_0402, antmicro-footprints:0402-res, F.Cu at (83.9, 37.7)
- added R75: R_200k_0402, antmicro-footprints:0402-res, F.Cu at (88.2, 33.9)
- added R76: R_100k_0402, antmicro-footprints:0402-res, F.Cu at (94.7, 29.1)
- added R77: R_124k_0402, antmicro-footprints:0402-res, F.Cu at (88.2, 35.9)
- added R78: R_100k_0402, antmicro-footprints:0402-res, F.Cu at (86.9, 31.9)
- added R79: R_124k_0402, antmicro-footprints:0402-res, F.Cu at (85.3, 35.2)
- added R80: R_100k_0402, antmicro-footprints:0402-res, F.Cu at (91.2, 33.7)
- added R81: R_10R_0603, antmicro-footprints:0603-res, F.Cu at (33.7, 60.2)
- added R82: R_47k_0402, antmicro-footprints:0402-res, F.Cu at (34.4, 62.5)
- added R83: R_453k_0402, antmicro-footprints:0402-res, F.Cu at (29.4, 67.4)
- added R84: R_100k_0402, antmicro-footprints:0402-res, F.Cu at (36.4, 64.5)
- added R85: R_4k7_0402, antmicro-footprints:0402-res, F.Cu at (43.1, 53.9)
- added R86: R_10k_0402, antmicro-footprints:0402-res, F.Cu at (46.0, 57.4)
- added R87: R_470k_0402, antmicro-footprints:0402-res, F.Cu at (48.9, 54.1)
- added R88: R_10k_0402, antmicro-footprints:0402-res, F.Cu at (39.3, 63.8)
- added R89: R_10k_0402, antmicro-footprints:0402-res, F.Cu at (40.2, 61.8)
- added R90: R_10k_0402, antmicro-footprints:0402-res, F.Cu at (48.9, 52.1)
- added R91: R_10k_0402, antmicro-footprints:0402-res, F.Cu at (36.4, 66.5)
- added R92: R_10k_0402, antmicro-footprints:0402-res, F.Cu at (43.0, 59.8)
- added R93: R_10k_0402, antmicro-footprints:0402-res, F.Cu at (37.2, 59.5)
- added R94: R_10k_0402, antmicro-footprints:0402-res, F.Cu at (46.0, 55.4)
- added R95: R_10k_0402, antmicro-footprints:0402-res, F.Cu at (43.0, 57.8)
- added R96: R_1k_0402, antmicro-footprints:0402-res, F.Cu at (33.4, 65.0)
- added R97: R_1k_0402, antmicro-footprints:0402-res, F.Cu at (46.0, 53.4)
- added R98: R_1k_0402, antmicro-footprints:0402-res, F.Cu at (32.3, 66.9)
- added R99: R_1k_0402, antmicro-footprints:0402-res, F.Cu at (37.3, 61.8)
- added TP2: TP_SMD1MM, antmicro-footprints:Testpoint_smd_1mm, F.Cu at (38.8, 65.8)
- added U10: TPS62823DLCT, antmicro-footprints:QFN-8_2x1mm, F.Cu at (98.5, 77.1)
- added U13: TPS62823DLCT, antmicro-footprints:QFN-8_2x1mm, F.Cu at (98.5, 90.5)
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- renumbered C96 to C1, C109 to C10, C117 to C11, C103 to C12, C110 to C13, C118 to C14, C104 to C15, C111 to C16, C119 to C17, C105 to C18, C106 to C19, C97 to C2, C120 to C20, C107 to C21, C112 to C22, C108 to C23, C113 to C24, C114 to C25, C121 to C26, C178 to C27, C180 to C28, C179 to C29, C98 to C3, C181 to C30, C182 to C31, C183 to C32, C184 to C33, C185 to C34, C177 to C35, C176 to C36, C175 to C37, C174 to C38, C173 to C39, C99 to C4, C164 to C40, C165 to C41, C171 to C42, C166 to C43, C172 to C44, C167 to C45, C168 to C46, C170 to C47, C149 to C48, C150 to C49, C100 to C5, C156 to C50, C151 to C51, C157 to C52, C152 to C53, C158 to C54, C153 to C55, C159 to C56, C162 to C57, C154 to C58, C160 to C59, C115 to C6, C155 to C60, C161 to C61, C163 to C62, C169 to C63, C101 to C7, C116 to C8, C102 to C9, D9 to D1, FB7 to FB1, FB6 to FB2, FB8 to FB3, J12 to J2, J11 to J3, J9 to J4, J7 to J5, J4 to J6, J5 to J7, J6 to J9, R5 to R1, R14 to R10, R15 to R11, R16 to R12, R4 to R13, R3 to R14, R1 to R15, R2 to R16, R92 to R17, R95 to R18, R93 to R19, R6 to R2, R94 to R20, R86 to R21, R80 to R22, R74 to R23, R64 to R24, R87 to R25, R81 to R26, R75 to R27, R65 to R28, R88 to R29, R7 to R3, R82 to R30, R76 to R31, R66 to R32, R89 to R33, R83 to R34, R77 to R35, R67 to R36, R90 to R37, R84 to R38, R78 to R39, R8 to R4, R68 to R40, R91 to R41, R85 to R42, R79 to R43, R69 to R44, R56 to R45, R60 to R46, R57 to R47, R61 to R48, R58 to R49, R9 to R5, R62 to R50, R59 to R51, R63 to R52, R55 to R53, R47 to R54, R50 to R55, R54 to R56, R53 to R57, R52 to R58, R51 to R59, R10 to R6, R46 to R60, R48 to R61, R49 to R62, R11 to R7, R12 to R8, R13 to R9, U2 to U1, U19 to U2, U18 to U3, U17 to U4, U16 to U5, U15 to U6, U13 to U7, U14 to U8
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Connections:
- C1 pad 1: VCC -> VCC1V2
- C12 pad 1: VCC -> VCC1V2
- C122 pad 1: VCC5V0 -> VCCA1
- C123 pad 1: VCC3V3 -> VCCAUX
- C123 pad 2: Net-(C123-Pad2) -> GND
- C124 pad 1: VCC3V3 -> VCC
- C125 pad 1: VCC3V3 -> VCCA1
- C126 pad 1: Net-(C126-Pad1) -> VCCAUX
- C126 pad 2: Net-(C126-Pad2) -> GND
- C127 pad 1: Net-(C127-Pad1) -> VCC
- C128 pad 1: Net-(C127-Pad1) -> VCCA1
- C129 pad 1: Net-(C127-Pad1) -> VCCAUX
- C133 pad 1: Net-(C133-Pad1) -> VCC
- C134 pad 1: Net-(C134-Pad1) -> VCCA1
- C135 pad 1: Net-(C135-Pad1) -> VCCAUX
- C136 pad 1: VCC5V0 -> VCC
- C137 pad 1: VCC1V8 -> VCCA1
- C137 pad 2: Net-(C137-Pad2) -> GND
- C138 pad 1: VCC1V8 -> VCCAUX
- C139 pad 1: VCC1V8 -> VCC
- C140 pad 1: VCC5V0 -> VCCAUX
- C141 pad 1: VCC1V35 -> VCC
- C141 pad 2: Net-(C141-Pad2) -> GND
- C142 pad 1: VCC1V35 -> VCCAUX
- C143 pad 1: VCC1V35 -> VCC
- C144 pad 1: VCC5V0 -> VCCAUX
- C145 pad 1: VCC1V0 -> VCC
- C145 pad 2: Net-(C145-Pad2) -> GND
- C146 pad 1: VCC1V0 -> VCC
- C147 pad 1: VCC1V0 -> VCC
- C148 pad 1: Net-(C148-Pad1) -> VCC
- C15 pad 1: VCC -> VCC1V2
- C2 pad 1: VCC -> VCC1V2
- C3 pad 1: VCC -> VCC1V2
- C4 pad 1: VCC -> VCC1V2
- C5 pad 1: VCC -> VCC1V2
- C64 pad 1: VCCA1 -> Net-(C64-Pad1)
- C68 pad 1: VCCA1 -> Net-(C68-Pad1)
- C69 pad 1: VCCA1 -> Net-(C69-Pad1)
- C7 pad 1: VCC -> VCC1V2
- C70 pad 1: VCCA1 -> Net-(C70-Pad1)
- C71 pad 1: VCCA1 -> Net-(C71-Pad1)
- C71 pad 2: GND -> Net-(C71-Pad2)
- C72 pad 1: /FPGA power supply/VCCHTX0 -> Net-(C72-Pad1)
- C73 pad 1: /FPGA power supply/VCCHTX0 -> Net-(C72-Pad1)
- C74 pad 1: /FPGA power supply/VCCHTX0 -> Net-(C72-Pad1)
- C75 pad 1: /FPGA power supply/VCCHTX0 -> VCC5V0
- C76 pad 1: VCCA0 -> VCC5V0
- C77 pad 1: VCCA0 -> VCC5V0
- C78 pad 1: VCCAUX -> VCC5V0
- C79 pad 1: VCCAUX -> VCC3V3
- C79 pad 2: GND -> Net-(C79-Pad2)
- C80 pad 1: VCCAUX -> VCC1V8
- C80 pad 2: GND -> Net-(C80-Pad2)
- C81 pad 1: VCCAUX -> VCC1V0
- C81 pad 2: GND -> Net-(C81-Pad2)
- C82 pad 1: VCCAUX -> VCC1V35
- C82 pad 2: GND -> Net-(C82-Pad2)
- C83 pad 1: VCCAUX -> VCC3V3
- C84 pad 1: VCCAUX -> VCC1V8
- C85 pad 1: VCCAUX -> VCC1V0
- C86 pad 1: VCCAUX -> VCC1V35
- C87 pad 1: VCCAUX -> VCC3V3
- C88 pad 1: VCCAUX -> VCC1V8
- C89 pad 1: VCCAUX -> VCC1V0
- C9 pad 1: VCC -> VCC1V2
- C90 pad 1: /FPGA power supply/VCCHTX1 -> VCC1V35
- C91 pad 1: /FPGA power supply/VCCHTX1 -> VCCA0
- C92 pad 1: /FPGA power supply/VCCHTX1 -> VCCA0
- C93 pad 1: /FPGA power supply/VCCHTX1 -> VCCA0
- C94 pad 1: VCCA1 -> VCCA0
- C95 pad 1: VCCA1 -> VCCA0
- F1 pad 1: Net-(F1-Pad1) -> PCIe_12V
- F2 pad 1: PCIe_12V -> Net-(F2-Pad1)
- FB2 pad 2: VCC -> VCC1V2
- FB3 pad 2: VCC -> VCC1V2
- FB4 pad 1: VCCAUX -> VCC
- FB4 pad 2: VCC2V5 -> VCCA0
- FB5 pad 1: VCC1V2T -> VCC
- FB5 pad 2: /FPGA power supply/VCCHTX1 -> /FPGA power supply/VCCHTX0
- IC1 pad 1: Net-(C126-Pad2) -> Net-(C71-Pad2)
- IC1 pad 4: Net-(C133-Pad1) -> Net-(C69-Pad1)
- IC1 pad 7: Net-(C135-Pad1) -> Net-(C70-Pad1)
- IC1 pad 9: Net-(C126-Pad1) -> Net-(C71-Pad1)
- J10 pad 1: PCICLK -> Net-(F2-Pad1)
- J10 pad 3: FRAME -> GND
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
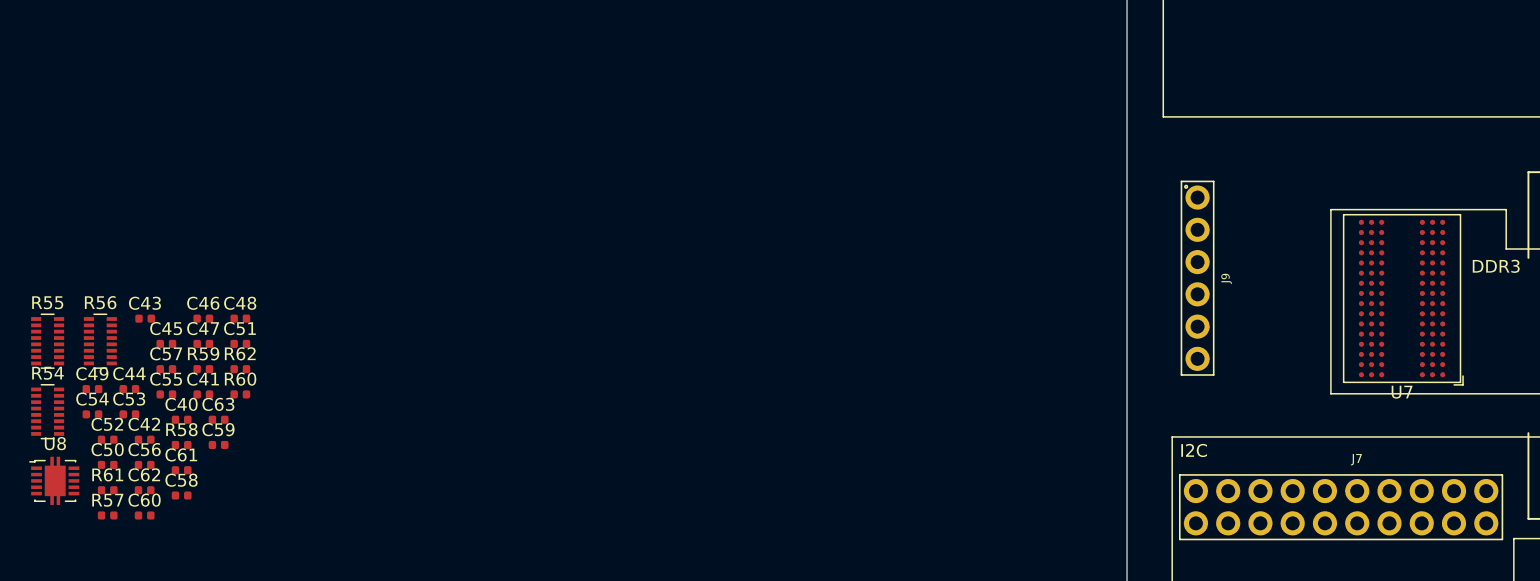
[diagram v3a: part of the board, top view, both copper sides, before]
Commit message: Update all schematic designators
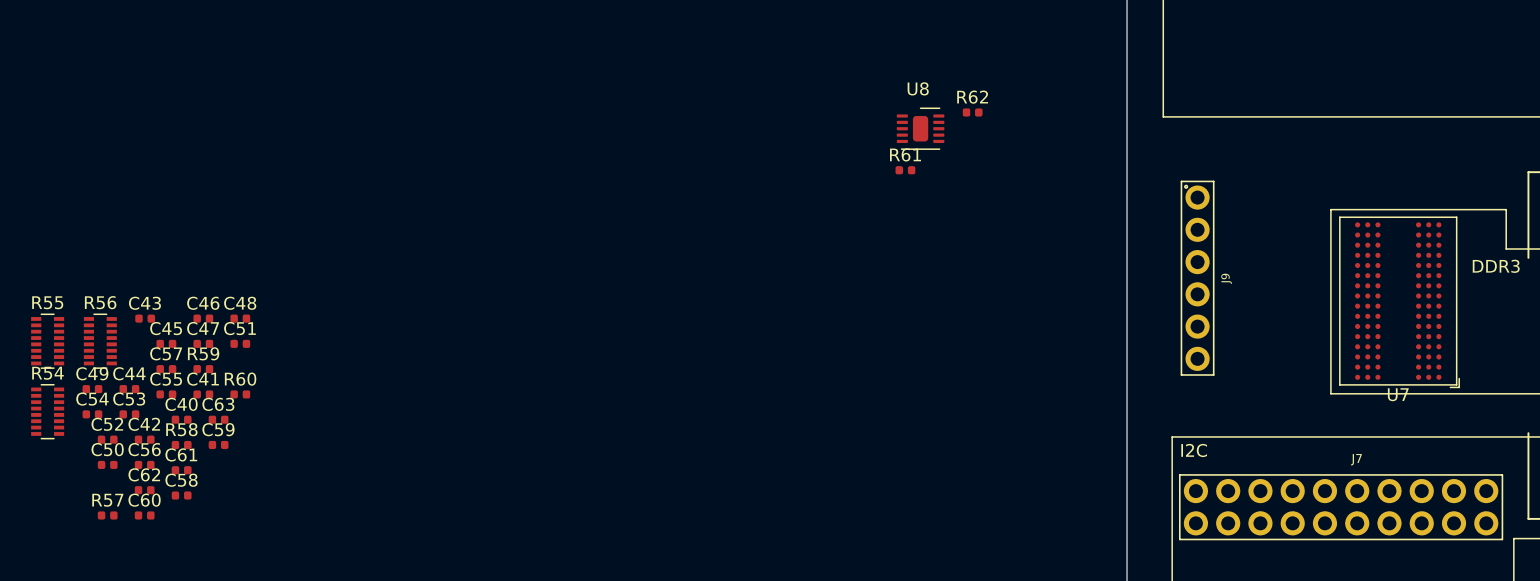
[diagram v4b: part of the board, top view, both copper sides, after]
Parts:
- R61, R62: value 51 -> R_51R_0402; footprint Resistor_SMD:R_0402_1005Metric -> antmicro-footprints:0402-res
- U8: footprint Package_SON:VSON-10-1EP_3x3mm_P0.5mm_EP1.65x2.4mm -> antmicro-footprints:VSON-10-1EP_3x3mm
- moved U8 73.3 mm to (43.7, 102.6)
- moved R61 67.7 mm to (42.7, 105.7)
- moved R62 61.1 mm to (48.0, 101.2)
- moved U7 0.36 mm to (81.5, 116.0)
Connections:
- net DDR3_Vref renamed DDR3_VREF
- net DDR3_Vtt_EN renamed DDR3_VTT_EN
- C40 pad 1: VCC1V35 -> /DDR3/DDR3_VTT
- C41 pad 1: VCC1V35 -> /DDR3/DDR3_VTT
- C43 pad 1: VCC1V35 -> /DDR3/DDR3_VTT
- U8 pad 3: VCC1V35 -> /DDR3/DDR3_VTT

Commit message: Fix designators
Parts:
- added J4: M20-7830642, antmicro-footprints:PinHeader_6x2_P2.54mm_Vertical, F.Cu at (115.2, 150.4)
- renumbered J9 to J10, J10 to J11, J11 to J12, J4 to J5, J5 to J6, J6 to J7, J7 to J8, J8 to J9
